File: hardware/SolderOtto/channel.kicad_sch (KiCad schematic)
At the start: 27 parts, among them J601 Conn_01x07, X601 Binder_IP40_07, X602 Binder_IP40_06, X603 Binder_IP40_07, X604 Hirose RPC1-12RB-6P, X605 Binder_IP40_07, X606 Hirose RPC1-12RB-6P

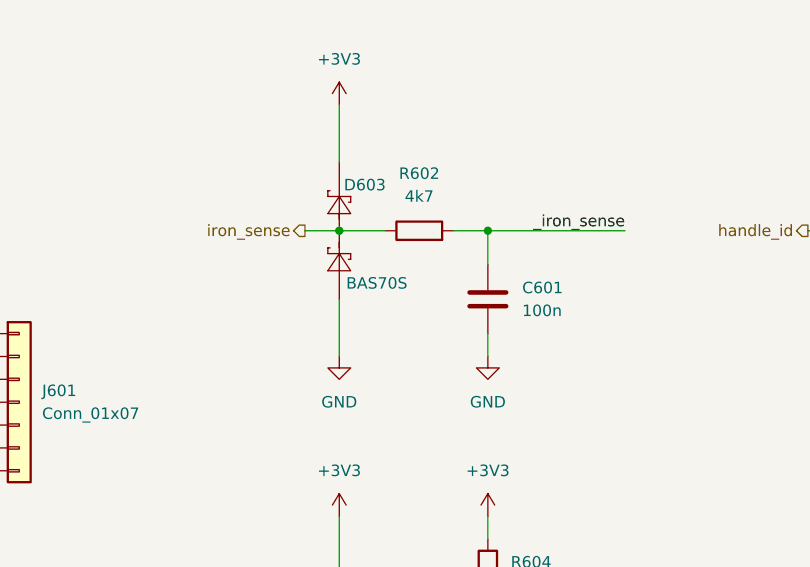
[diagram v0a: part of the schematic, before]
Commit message: fix some part numbers
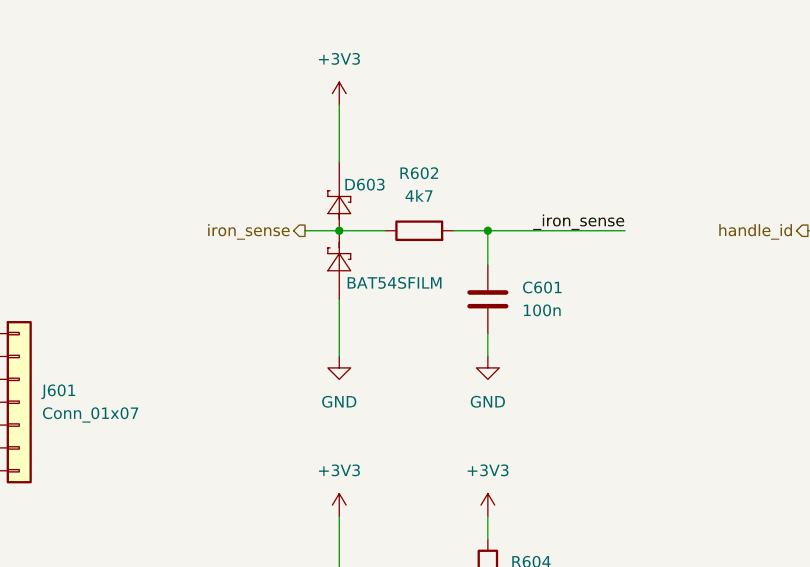
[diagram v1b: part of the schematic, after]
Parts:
- D603: value BAS70S -> BAT54SFILM; Mouser 511-BAT54SFILM -> (none)
- D604, D605, D606: Mouser 511-BAT54SFILM -> (none)
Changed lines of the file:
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@@
 	)
 	(junction
+		(at 190.5 90.17)
+		(diameter 0)
+		(color 0 0 0 0)
+	)
+	(junction
 		(at 262.89 90.17)
 		(diameter 0)
@@
 	)
 	(junction
-		(at 190.5 90.17)
-		(diameter 0)
-		(color 0 0 0 0)
-	)
-	(junction
 		(at 60.96 153.67)
 		(diameter 0)
@@
 	(wire
 		(pts
-			(xy 190.5 90.17) (xy 195.58 90.17)
+			(xy 186.69 90.17) (xy 190.5 90.17)
 		)
 		(stroke
@@
 	(wire
 		(pts
+			(xy 190.5 90.17) (xy 195.58 90.17)
+		)
+		(stroke
+			(width 0)
+			(type default)
+		)
+	)
+	(wire
+		(pts
 			(xy 66.04 86.36) (xy 66.04 77.47)
 		)
@@
 	(wire
 		(pts
-			(xy 186.69 90.17) (xy 190.5 90.17)
-		)
-		(stroke
-			(width 0)
-			(type default)
-		)
-	)
-	(wire
-		(pts
 			(xy 207.01 121.92) (xy 207.01 124.46)
 		)
@@
 	)
 	(symbol
+		(lib_id "mylib_diodes:BAT54SFILM")
+		(at 190.5 90.17 90)
+		(unit 1)
+		(exclude_from_sim yes)
+		(in_bom yes)
+		(on_board yes)
+		(dnp no)
+		(property "Reference" "D603"
+			(at 191.008 85.09 90)
+			(effects
+				(font
+					(size 1.27 1.27)
+				)
+				(justify right)
+			)
+		)
+		(property "Value" "BAT54SFILM"
+			(at 191.262 96.012 90)
+			(effects
+				(font
+					(size 1.27 1.27)
+				)
+				(justify right)
+			)
+		)
+		(property "Footprint" "Package_TO_SOT_SMD:SOT-23"
+			(at 190.5 90.17 0)
+			(effects
+				(font
+					(size 1.27 1.27)
+				)
+				(hide yes)
+			)
+		)
+		(property "Datasheet" ""
+			(at 190.5 90.17 0)
+			(effects
+				(font
+					(size 1.27 1.27)
+				)
+				(hide yes)
+			)
+		)
+		(property "Description" ""
+			(at 190.5 90.17 0)
+			(effects
+				(font
+					(size 1.27 1.27)
+				)
+				(hide yes)
+			)
+		)
+		(property "Digikey" "497-2522-1-ND"
+			(at 193.04 92.7099 90)
+			(effects
+				(font
+					(size 1.27 1.27)
+				)
+				(justify right)
+				(hide yes)
+			)
+		)
+		(pin "3"
+		)
+		(pin "2"
+		)
+		(pin "1"
+		)
+		(instances
+			(project "SolderOtto"
+				(path "/04e99464-bf33-4a4f-8397-d26b5ec904f3/57a4c2b0-a7ab-4dc9-9bcc-6bd7e1b882d1"
+					(reference "D603")
+					(unit 1)
+				)
+			)
+		)
+	)
+	(symbol
 		(lib_id "mylib_connectors:JBC-AM120")
 		(at 100.33 86.36 0)
@@
 			)
 		)
-		(property "Mouser" "511-BAT54SFILM"
-			(at 190.5 135.89 0)
-			(effects
-				(font
-					(size 1.27 1.27)
-				)
-				(hide yes)
-			)
-		)
 		(pin "3"
 		)
@@
 			)
 		)
-		(property "Mouser" "511-BAT54SFILM"
-			(at 246.38 135.89 0)
-			(effects
-				(font
-					(size 1.27 1.27)
-				)
-				(hide yes)
-			)
-		)
 		(pin "3"
 		)
@@
 			)
 		)
-		(property "Mouser" "511-BAT54SFILM"
-			(at 246.38 90.17 0)
-			(effects
-				(font
-					(size 1.27 1.27)
-				)
-				(hide yes)
-			)
-		)
 		(pin "3"
 		)
@@
 					(unit 1)
 				)
-			)
-		)
-	)
-	(symbol
-		(lib_id "mylib_diodes:BAT54SFILM")
-		(at 190.5 90.17 90)
-		(unit 1)
-		(exclude_from_sim yes)
-		(in_bom yes)
-		(on_board yes)
-		(dnp no)
-		(property "Reference" "D603"
-			(at 191.008 85.09 90)
-			(effects
-				(font
-					(size 1.27 1.27)
-				)
-				(justify right)
-			)
-		)
-		(property "Value" "BAS70S"
-			(at 191.262 96.012 90)
-			(effects
-				(font
-					(size 1.27 1.27)
-				)
-				(justify right)
-			)
-		)
-		(property "Footprint" "Package_TO_SOT_SMD:SOT-23"
-			(at 190.5 90.17 0)
-			(effects
-				(font
-					(size 1.27 1.27)
-				)
-				(hide yes)
-			)
-		)
-		(property "Datasheet" ""
-			(at 190.5 90.17 0)
-			(effects
-				(font
-					(size 1.27 1.27)
-				)
-				(hide yes)
-			)
-		)
-		(property "Description" ""
-			(at 190.5 90.17 0)
-			(effects
-				(font
-					(size 1.27 1.27)
-				)
-				(hide yes)
-			)
-		)
-		(property "Digikey" "497-2522-1-ND"
-			(at 193.04 92.7099 90)
-			(effects
-				(font
-					(size 1.27 1.27)
-				)
-				(justify right)
-				(hide yes)
-			)
-		)
-		(property "Mouser" "511-BAT54SFILM"
-			(at 190.5 90.17 0)
-			(effects
-				(font
-					(size 1.27 1.27)
-				)
-				(hide yes)
-			)
-		)
-		(pin "3"
-		)
-		(pin "2"
-		)
-		(pin "1"
-		)
-		(instances
-			(project "SolderOtto"
-				(path "/04e99464-bf33-4a4f-8397-d26b5ec904f3/57a4c2b0-a7ab-4dc9-9bcc-6bd7e1b882d1"
-					(reference "D603")
-					(unit 1)
-				)

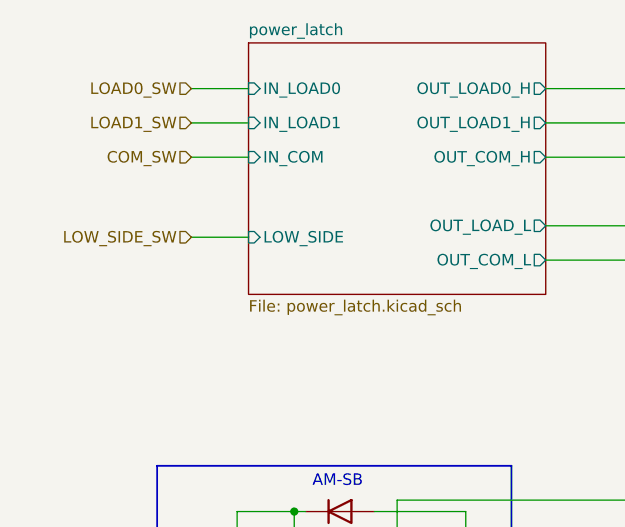
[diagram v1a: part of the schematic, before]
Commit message: remove low side switching ic
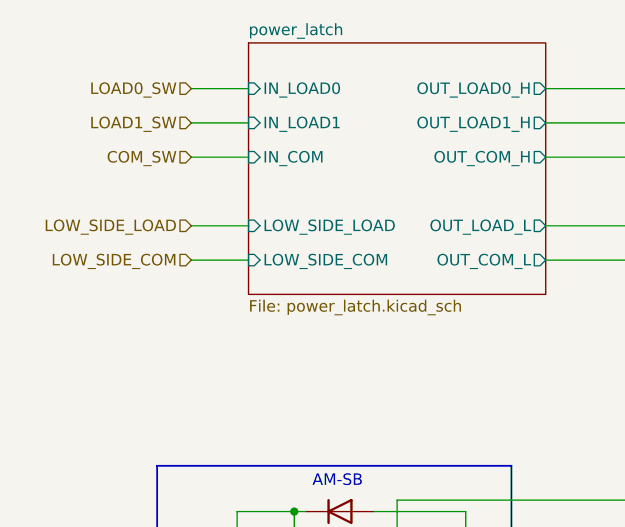
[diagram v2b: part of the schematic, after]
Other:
- sheet power_latch ports: added LOW_SIDE_COM, LOW_SIDE_LOAD; removed LOW_SIDE
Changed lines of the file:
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@@
 	(wire
 		(pts
+			(xy 35.56 49.53) (xy 41.91 49.53)
+		)
+		(stroke
+			(width 0)
+			(type default)
+		)
+	)
+	(wire
+		(pts
 			(xy 62.23 81.28) (xy 62.23 83.82)
 		)
@@
 	(wire
 		(pts
-			(xy 35.56 46.99) (xy 41.91 46.99)
+			(xy 35.56 45.72) (xy 41.91 45.72)
 		)
 		(stroke
@@
 		)
 	)
+	(hierarchical_label "LOW_SIDE_COM"
+		(shape input)
+		(at 35.56 49.53 180)
+		(fields_autoplaced yes)
+		(effects
+			(font
+				(size 1.27 1.27)
+			)
+			(justify right)
+		)
+	)
 	(hierarchical_label "T_{TIP}"
 		(shape output)
@@
 		)
 	)
-	(hierarchical_label "LOW_SIDE_SW"
+	(hierarchical_label "LOW_SIDE_LOAD"
 		(shape input)
-		(at 35.56 46.99 180)
+		(at 35.56 45.72 180)
 		(fields_autoplaced yes)
 		(effects
@@
 			)
 		)
-		(pin "LOW_SIDE" input
-			(at 41.91 46.99 180)
+		(pin "OUT_LOAD1_H" output
+			(at 74.93 34.29 0)
+			(effects
+				(font
+					(size 1.27 1.27)
+				)
+				(justify right)
+			)
+		)
+		(pin "LOW_SIDE_LOAD" input
+			(at 41.91 45.72 180)
 			(effects
 				(font
@@
 			)
 		)
-		(pin "OUT_LOAD1_H" output
-			(at 74.93 34.29 0)
+		(pin "LOW_SIDE_COM" input
+			(at 41.91 49.53 180)
 			(effects
 				(font
 					(size 1.27 1.27)
 				)
-				(justify right)
+				(justify left)
 			)
 		)

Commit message: rework pcb
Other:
- sheet channel_meas ports: added SEL1_{a}, SEL1_{b}, SEL2_{a}, SEL2_{b}, T_{TIP}_{a}, T_{TIP}_{b}; removed DET, SEL1, SEL2, SEL3, T_{TIP}
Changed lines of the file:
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@@
 	(wire
 		(pts
-			(xy 152.4 29.21) (xy 157.48 29.21)
+			(xy 152.4 27.94) (xy 157.48 27.94)
 		)
 		(stroke
@@
 	(wire
 		(pts
-			(xy 193.04 33.02) (xy 205.74 33.02)
+			(xy 193.04 30.48) (xy 205.74 30.48)
 		)
 		(stroke
@@
 	(wire
 		(pts
-			(xy 193.04 49.53) (xy 201.93 49.53)
-		)
-		(stroke
-			(width 0)
-			(type default)
-		)
-	)
-	(wire
-		(pts
 			(xy 35.56 49.53) (xy 41.91 49.53)
 		)
@@
 	(wire
 		(pts
-			(xy 152.4 34.29) (xy 157.48 34.29)
+			(xy 152.4 33.02) (xy 157.48 33.02)
 		)
 		(stroke
@@
 	(wire
 		(pts
-			(xy 193.04 44.45) (xy 201.93 44.45)
+			(xy 193.04 43.18) (xy 205.74 43.18)
 		)
 		(stroke
@@
 	(wire
 		(pts
-			(xy 193.04 38.1) (xy 205.74 38.1)
+			(xy 193.04 35.56) (xy 205.74 35.56)
 		)
 		(stroke
@@
 	(wire
 		(pts
-			(xy 193.04 35.56) (xy 205.74 35.56)
+			(xy 193.04 33.02) (xy 205.74 33.02)
 		)
 		(stroke
@@
 	(wire
 		(pts
-			(xy 193.04 46.99) (xy 201.93 46.99)
+			(xy 193.04 45.72) (xy 205.74 45.72)
+		)
+		(stroke
+			(width 0)
+			(type default)
+		)
+	)
+	(wire
+		(pts
+			(xy 152.4 35.56) (xy 157.48 35.56)
 		)
 		(stroke
@@
 	(wire
 		(pts
-			(xy 193.04 41.91) (xy 201.93 41.91)
+			(xy 193.04 40.64) (xy 205.74 40.64)
 		)
 		(stroke
@@
 	(wire
 		(pts
-			(xy 193.04 30.48) (xy 205.74 30.48)
+			(xy 193.04 27.94) (xy 205.74 27.94)
 		)
 		(stroke
@@
 	(wire
 		(pts
-			(xy 152.4 31.75) (xy 157.48 31.75)
+			(xy 152.4 30.48) (xy 157.48 30.48)
 		)
 		(stroke
@@
 	(wire
 		(pts
+			(xy 193.04 48.26) (xy 205.74 48.26)
+		)
+		(stroke
+			(width 0)
+			(type default)
+		)
+	)
+	(wire
+		(pts
 			(xy 149.86 104.14) (xy 134.62 104.14)
 		)
@@
 	)
 	(label "LOAD"
-		(at 205.74 35.56 180)
+		(at 205.74 33.02 180)
 		(fields_autoplaced yes)
 		(effects
@@
 	)
 	(label "TC"
-		(at 205.74 30.48 180)
+		(at 205.74 27.94 180)
 		(fields_autoplaced yes)
 		(effects
@@
 	)
 	(label "COM"
-		(at 205.74 33.02 180)
+		(at 205.74 30.48 180)
 		(fields_autoplaced yes)
 		(effects
@@
 	)
 	(label "_iron_sense"
-		(at 205.74 38.1 180)
+		(at 205.74 35.56 180)
 		(fields_autoplaced yes)
 		(effects
@@
 		)
 	)
-	(hierarchical_label "T_{TIP}"
-		(shape output)
-		(at 201.93 46.99 0)
-		(fields_autoplaced yes)
-		(effects
-			(font
-				(size 1.27 1.27)
-			)
-			(justify left)
-		)
-	)
-	(hierarchical_label "DET"
-		(shape output)
-		(at 201.93 49.53 0)
+	(hierarchical_label "T_{TIP}_{a}"
+		(shape passive)
+		(at 205.74 45.72 0)
 		(fields_autoplaced yes)
 		(effects
@@
 		)
 	)
+	(hierarchical_label "T_{TIP}_{b}"
+		(shape passive)
+		(at 205.74 48.26 0)
+		(fields_autoplaced yes)
+		(effects
+			(font
+				(size 1.27 1.27)
+			)
+			(justify left)
+		)
+	)
 	(hierarchical_label "I_{LOAD}"
-		(shape output)
-		(at 201.93 41.91 0)
+		(shape passive)
+		(at 205.74 40.64 0)
 		(fields_autoplaced yes)
 		(effects
@@
 	)
 	(hierarchical_label "handle_id"
-		(shape output)
+		(shape passive)
 		(at 242.57 90.17 180)
 		(fields_autoplaced yes)
@@
 	)
 	(hierarchical_label "I_{LEAK}"
-		(shape output)
-		(at 201.93 44.45 0)
+		(shape passive)
+		(at 205.74 43.18 0)
 		(fields_autoplaced yes)
 		(effects
@@
 		)
 	)
-	(hierarchical_label "SEL3"
+	(hierarchical_label "SEL1_{b}"
 		(shape input)
-		(at 152.4 34.29 180)
+		(at 152.4 33.02 180)
 		(fields_autoplaced yes)
 		(effects
@@
 		)
 	)
+	(hierarchical_label "SEL2_{b}"
+		(shape input)
+		(at 152.4 35.56 180)
+		(fields_autoplaced yes)
+		(effects
+			(font
+				(size 1.27 1.27)
+			)
+			(justify right)
+		)
+	)
 	(hierarchical_label "LOAD1_SW"
 		(shape input)
@@
 		)
 	)
-	(hierarchical_label "SEL2"
+	(hierarchical_label "SEL2_{a}"
 		(shape input)
-		(at 152.4 31.75 180)
+		(at 152.4 30.48 180)
 		(fields_autoplaced yes)
 		(effects
@@
 		)
 	)
-	(hierarchical_label "SEL1"
+	(hierarchical_label "SEL1_{a}"
 		(shape input)
-		(at 152.4 29.21 180)
+		(at 152.4 27.94 180)
 		(fields_autoplaced yes)
 		(effects
@@
 		)
 		(pin "COM" bidirectional
-			(at 193.04 33.02 0)
+			(at 193.04 30.48 0)
 			(effects
 				(font
@@
 		)
 		(pin "TC" bidirectional
-			(at 193.04 30.48 0)
+			(at 193.04 27.94 0)
 			(effects
 				(font
@@
 			)
 		)
-		(pin "DET" input
-			(at 193.04 49.53 0)
+		(pin "I_{LEAK}" passive
+			(at 193.04 43.18 0)
 			(effects
 				(font
@@
 			)
 		)
-		(pin "SEL3" input
-			(at 157.48 34.29 180)
+		(pin "I_{LOAD}" passive
+			(at 193.04 40.64 0)
 			(effects
 				(font
 					(size 1.27 1.27)
 				)
-				(justify left)
+				(justify right)
 			)
 		)
-		(pin "SEL2" input
-			(at 157.48 31.75 180)
+		(pin "LOAD1" bidirectional
+			(at 193.04 35.56 0)
 			(effects
 				(font
 					(size 1.27 1.27)
 				)
-				(justify left)
+				(justify right)
 			)
 		)
-		(pin "I_{LEAK}" input
-			(at 193.04 44.45 0)
+		(pin "LOAD0" bidirectional
+			(at 193.04 33.02 0)
 			(effects
 				(font
@@
 			)
 		)
-		(pin "I_{LOAD}" input
-			(at 193.04 41.91 0)
+		(pin "T_{TIP}_{b}" passive
+			(at 193.04 48.26 0)
 			(effects
 				(font
@@
 			)
 		)
-		(pin "T_{TIP}" input
-			(at 193.04 46.99 0)
+		(pin "T_{TIP}_{a}" passive
+			(at 193.04 45.72 0)
 			(effects
 				(font
@@
 			)
 		)
-		(pin "SEL1" input
-			(at 157.48 29.21 180)
+		(pin "SEL1_{b}" input
+			(at 157.48 30.48 180)
 			(effects
 				(font
@@
 			)
 		)
-		(pin "LOAD1" bidirectional
-			(at 193.04 38.1 0)
+		(pin "SEL2_{b}" input
+			(at 157.48 35.56 180)
 			(effects
 				(font
 					(size 1.27 1.27)
 				)
-				(justify right)
+				(justify left)
 			)
 		)
-		(pin "LOAD0" bidirectional
-			(at 193.04 35.56 0)
+		(pin "SEL1_{a}" input
+			(at 157.48 27.94 180)
 			(effects
 				(font
 					(size 1.27 1.27)
 				)
-				(justify right)
+				(justify left)
+			)
+		)
+		(pin "SEL2_{a}" input
+			(at 157.48 33.02 180)
+			(effects
+				(font
+					(size 1.27 1.27)
+				)
+				(justify left)
 			)
 		)

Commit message: save work
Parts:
- removed C601: 100n, Capacitor_SMD:C_0603_1608Metric, symbol Device:C
- removed D603: BAT54SFILM, Package_TO_SOT_SMD:SOT-23, symbol mylib_diodes:BAT54SFILM
- removed R602: 4k7, Resistor_SMD:R_0603_1608Metric, symbol Device:R

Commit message: rdy to route
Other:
- removed sheet power_latch
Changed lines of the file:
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@@
 	(wire
 		(pts
-			(xy 35.56 30.48) (xy 41.91 30.48)
+			(xy 86.36 30.48) (xy 100.33 30.48)
 		)
 		(stroke
@@
 	(wire
 		(pts
-			(xy 74.93 45.72) (xy 100.33 45.72)
-		)
-		(stroke
-			(width 0)
-			(type default)
-		)
-	)
-	(wire
-		(pts
 			(xy 91.44 153.67) (xy 74.93 153.67)
 		)
@@
 	(wire
 		(pts
-			(xy 35.56 38.1) (xy 41.91 38.1)
+			(xy 86.36 38.1) (xy 100.33 38.1)
 		)
 		(stroke
@@
 	(wire
 		(pts
-			(xy 35.56 49.53) (xy 41.91 49.53)
+			(xy 86.36 49.53) (xy 100.33 49.53)
 		)
 		(stroke
@@
 	(wire
 		(pts
-			(xy 35.56 45.72) (xy 41.91 45.72)
+			(xy 86.36 45.72) (xy 100.33 45.72)
 		)
 		(stroke
@@
 	(wire
 		(pts
-			(xy 35.56 34.29) (xy 41.91 34.29)
+			(xy 86.36 34.29) (xy 100.33 34.29)
 		)
 		(stroke
@@
 	(wire
 		(pts
-			(xy 74.93 34.29) (xy 100.33 34.29)
-		)
-		(stroke
-			(width 0)
-			(type default)
-		)
-	)
-	(wire
-		(pts
 			(xy 88.9 96.52) (xy 77.47 96.52)
 		)
@@
 	(wire
 		(pts
-			(xy 74.93 30.48) (xy 100.33 30.48)
-		)
-		(stroke
-			(width 0)
-			(type default)
-		)
-	)
-	(wire
-		(pts
-			(xy 74.93 38.1) (xy 100.33 38.1)
-		)
-		(stroke
-			(width 0)
-			(type default)
-		)
-	)
-	(wire
-		(pts
 			(xy 34.29 161.29) (xy 34.29 151.13)
 		)
@@
 	(wire
 		(pts
-			(xy 74.93 49.53) (xy 100.33 49.53)
-		)
-		(stroke
-			(width 0)
-			(type default)
-		)
-	)
-	(wire
-		(pts
 			(xy 48.26 153.67) (xy 60.96 153.67)
 		)
@@
 	(hierarchical_label "LOW_SIDE_COM"
 		(shape input)
-		(at 35.56 49.53 180)
+		(at 86.36 49.53 180)
 		(fields_autoplaced yes)
 		(effects
@@
 	(hierarchical_label "LOAD0_SW"
 		(shape input)
-		(at 35.56 30.48 180)
+		(at 86.36 30.48 180)
 		(fields_autoplaced yes)
 		(effects
@@
 	(hierarchical_label "COM_SW"
 		(shape input)
-		(at 35.56 38.1 180)
+		(at 86.36 38.1 180)
 		(fields_autoplaced yes)
 		(effects
@@
 	(hierarchical_label "LOW_SIDE_LOAD"
 		(shape input)
-		(at 35.56 45.72 180)
+		(at 86.36 45.72 180)
 		(fields_autoplaced yes)
 		(effects
@@
 	(hierarchical_label "LOAD1_SW"
 		(shape input)
-		(at 35.56 34.29 180)
+		(at 86.36 34.29 180)
 		(fields_autoplaced yes)
 		(effects
@@
 				)
 			)
-		)
-	)
-	(sheet
-		(at 41.91 25.4)
-		(size 33.02 27.94)
-		(fields_autoplaced yes)
-		(stroke
-			(width 0.1524)
-			(type solid)
-		)
-		(fill
-			(color 255 255 194 1.0000)
-		)
-		(property "Sheetname" "power_latch"
-			(at 41.91 24.6884 0)
-			(effects
-				(font
-					(size 1.27 1.27)
-				)
-				(justify left bottom)
-			)
-		)
-		(property "Sheetfile" "power_latch.kicad_sch"
-			(at 41.91 53.9246 0)
-			(effects
-				(font
-					(size 1.27 1.27)
-				)
-				(justify left top)
-			)
-		)
-		(pin "IN_COM" input
-			(at 41.91 38.1 180)
-			(effects
-				(font
-					(size 1.27 1.27)
-				)
-				(justify left)
-			)
-		)
-		(pin "OUT_COM_H" output
-			(at 74.93 38.1 0)
-			(effects
-				(font
-					(size 1.27 1.27)
-				)
-				(justify right)
-			)
-		)
-		(pin "OUT_LOAD_L" output
-			(at 74.93 45.72 0)
-			(effects
-				(font
-					(size 1.27 1.27)
-				)
-				(justify right)
-			)
-		)
-		(pin "OUT_COM_L" output
-			(at 74.93 49.53 0)
-			(effects
-				(font
-					(size 1.27 1.27)
-				)
-				(justify right)
-			)
-		)
-		(pin "OUT_LOAD0_H" output
-			(at 74.93 30.48 0)
-			(effects
-				(font
-					(size 1.27 1.27)
-				)
-				(justify right)
-			)
-		)
-		(pin "IN_LOAD1" input
-			(at 41.91 34.29 180)
-			(effects
-				(font
-					(size 1.27 1.27)
-				)
-				(justify left)
-			)
-		)
-		(pin "IN_LOAD0" input
-			(at 41.91 30.48 180)
-			(effects
-				(font
-					(size 1.27 1.27)
-				)
-				(justify left)
-			)
-		)
-		(pin "OUT_LOAD1_H" output
-			(at 74.93 34.29 0)
-			(effects
-				(font
-					(size 1.27 1.27)
-				)
-				(justify right)
-			)
-		)
-		(pin "LOW_SIDE_LOAD" input
-			(at 41.91 45.72 180)
-			(effects
-				(font
-					(size 1.27 1.27)
-				)
-				(justify left)
-			)
-		)
-		(pin "LOW_SIDE_COM" input
-			(at 41.91 49.53 180)
-			(effects
-				(font
-					(size 1.27 1.27)
-				)
-				(justify left)
-			)
-		)
-		(instances
-			(project "SolderOtto"
-				(path "/04e99464-bf33-4a4f-8397-d26b5ec904f3/57a4c2b0-a7ab-4dc9-9bcc-6bd7e1b882d1"
-					(page "7")
-				)
-			)
